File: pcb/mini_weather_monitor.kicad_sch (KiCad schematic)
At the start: 20 parts, among them U2 4.0inch_SPI_MSP4021, U2_BME280 module_bme280, U3_BH1750 module_bh1750

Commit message: working code. pcb wip
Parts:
- removed 5V_buck_boost1: ~, regulator_voltage:S09_HVN, symbol voltage_regulator:S09_HVN
- removed D2, D3, D4, D5, D6: 1N5819, Diode_SMD:D_SOD-123, symbol Diode:1N5819
- added C4: 100nF, Capacitor_SMD:C_1206_3216Metric_Pad1.33x1.80mm_HandSolder, symbol Device:C_Small
- added C5, C6, C7, C8: 10uF, Capacitor_SMD:C_1206_3216Metric_Pad1.33x1.80mm_HandSolder, symbol Device:C_Small
- added J1: Conn_01x02, Connector_PinHeader_2.54mm:PinHeader_1x02_P2.54mm_Vertical, symbol Connector_Generic:Conn_01x02
- added Q1: IRLML6402, Package_TO_SOT_SMD:SOT-23, symbol Transistor_FET:IRLML6402
- added R2: 1k, Resistor_SMD:R_1206_3216Metric, symbol Device:R
- added U1: ~, boost_converter:Pololu U3V70F5, symbol buck_converter:U3V70F5
- C1, C2, C3: value C_Small -> 100nF
- D1: footprint Diode_SMD:D_SOD-123 -> Diode_SMD:D_SMB
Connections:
- net +3V3: now also C4.1, C7.1
- net GND: now also C1.2, C2.2, C3.2, C4.2, C5.2, C6.2, C7.2, C8.2, R2.2, U1.2 (GND), U1.4 (GND)
- net VCC: now also C1.1, C3.1, U2.1 (VCC), U3_BH1750.5 (VCC), C5.1, C6.1, C8.1, U1.5 (VOUT); no longer C2.2
- net VBUS: now reaches D1.1 (K)
- net VBUS: now also Q1.2 (S), U1.3 (VIN)
- net at adafruit_type_c_breakout_rev_b1.2 (VBUS): now also adafruit_type_c_vertical_breakout1.10 (VBUS), adafruit_type_c_vertical_breakout1.2 (VBUS), Q1.3 (D)
- net at D1.2 (A): now also Q1.1 (G), R2.1; no longer adafruit_type_c_vertical_breakout1.2 (VBUS)
- net at U_ESP32_DEVKIT_V1.12 (RX0): now also J1.1 (Pin_1)
- net at U_ESP32_DEVKIT_V1.13 (TX0): now also J1.2 (Pin_2)
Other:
- moved on the sheet: C1, C3, H1, H2

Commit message: set mosfet, schottkey and resistor
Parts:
- D1: footprint Diode_SMD:D_SMB -> Diode_SMD:D_SOD-123
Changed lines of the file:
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@@
 			)
 		)
-		(property "Footprint" "Diode_SMD:D_SMB"
+		(property "Footprint" "Diode_SMD:D_SOD-123"
 			(at 31.75 63.5 0)
 			(effects

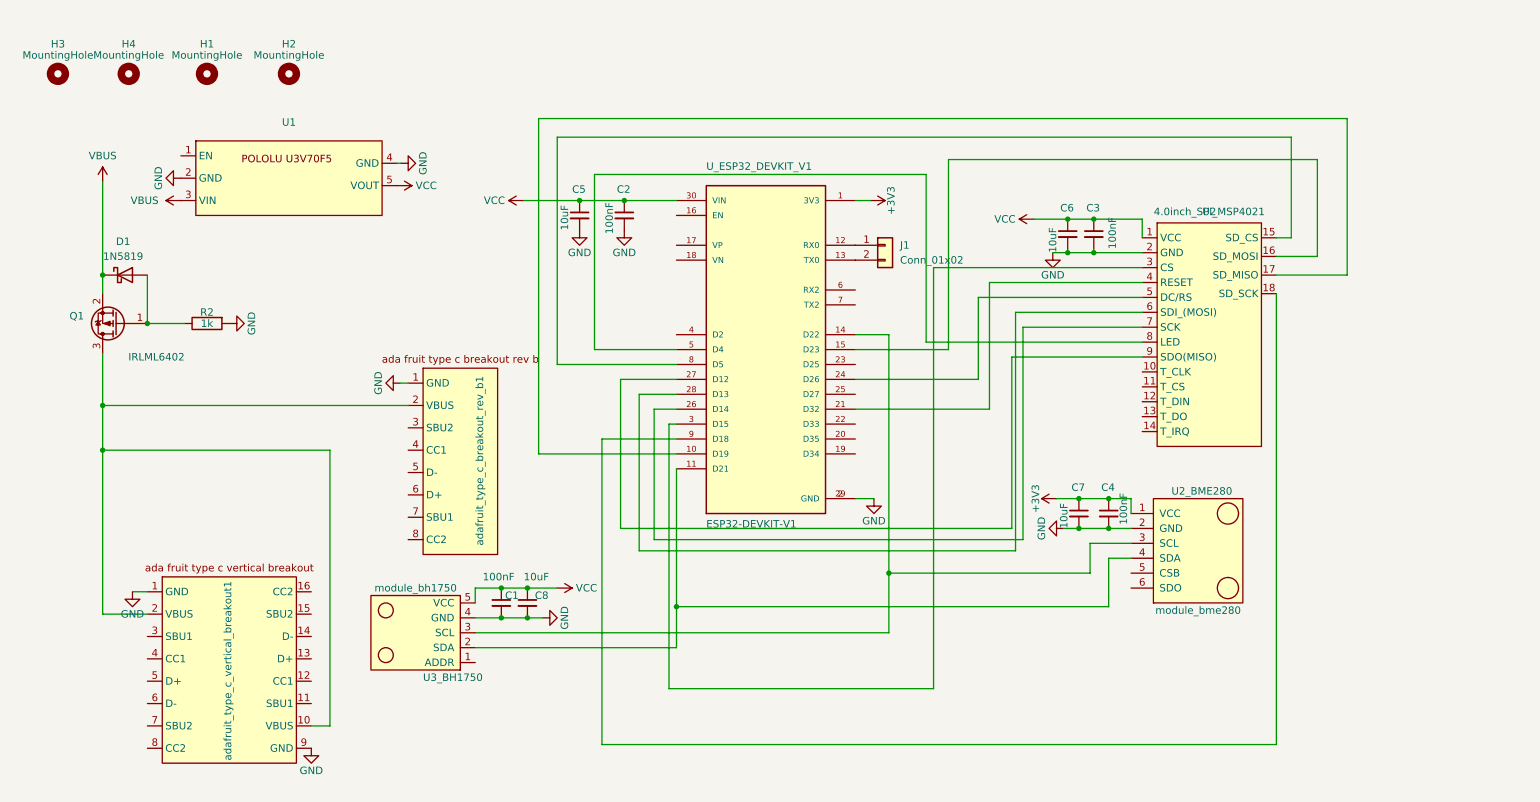
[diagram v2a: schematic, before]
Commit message: adding mini sdcard to use instead of onboard sdcard
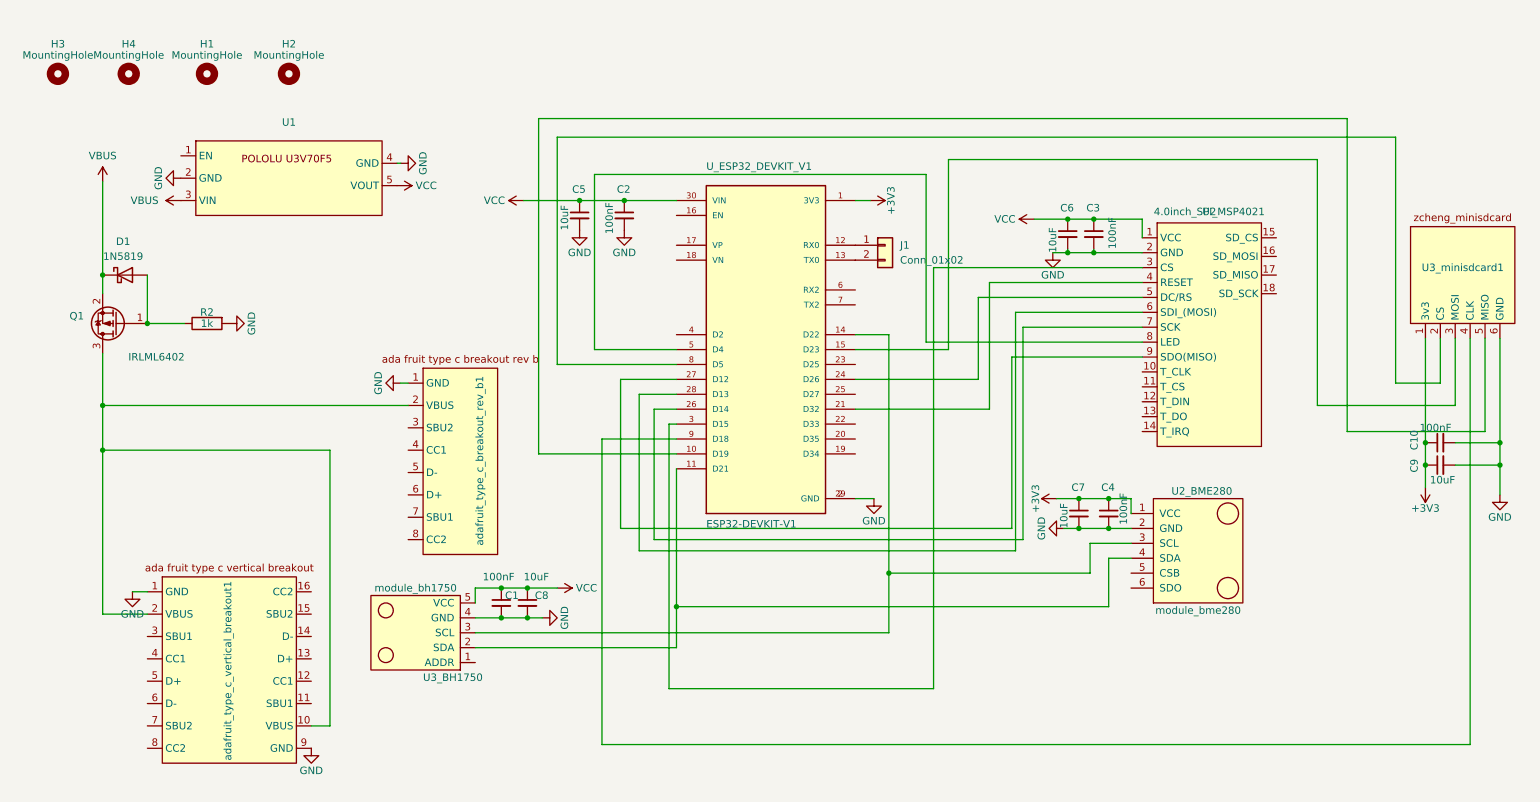
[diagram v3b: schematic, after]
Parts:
- added C10: 100nF, Capacitor_SMD:C_1206_3216Metric_Pad1.33x1.80mm_HandSolder, symbol Device:C_Small
- added C9: 10uF, Capacitor_SMD:C_1206_3216Metric_Pad1.33x1.80mm_HandSolder, symbol Device:C_Small
- added U3_minisdcard1: ~, mini_weather_monitor:zicheng_mini_sd_card_reader, symbol zicheng_minisdcard:zicheng_minisdcard
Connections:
- net +3V3: now also C10.1, C9.1, U3_minisdcard1.1 (3v3)
- net GND: now also C10.2, C9.2, U3_minisdcard1.6 (GND)
- net at U2.15 (SD_CS): no longer U_ESP32_DEVKIT_V1.8 (D5)
- net at U2.16 (SD_MOSI): no longer U_ESP32_DEVKIT_V1.15 (D23)
- net at U2.17 (SD_MISO): no longer U_ESP32_DEVKIT_V1.10 (D19)
- net at U2.18 (SD_SCK): no longer U_ESP32_DEVKIT_V1.9 (D18)
- new net: U3_minisdcard1.5 (MISO), U_ESP32_DEVKIT_V1.10 (D19)
- new net: U3_minisdcard1.3 (MOSI), U_ESP32_DEVKIT_V1.15 (D23)
- new net: U3_minisdcard1.2 (CS), U_ESP32_DEVKIT_V1.8 (D5)
- new net: U3_minisdcard1.4 (CLK), U_ESP32_DEVKIT_V1.9 (D18)

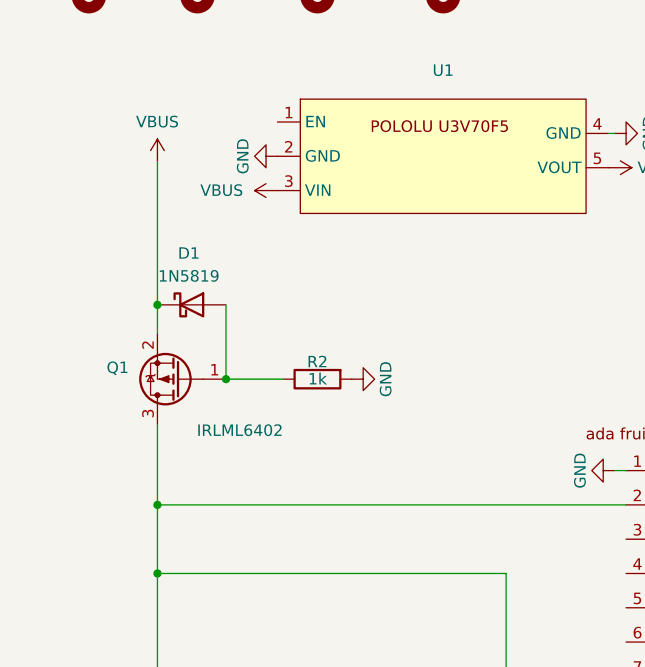
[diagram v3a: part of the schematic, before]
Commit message: moved config info to config on sdcard
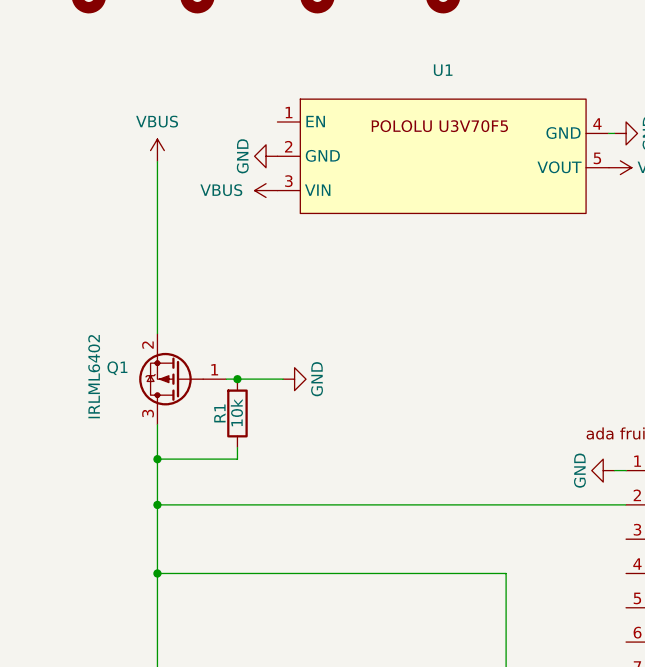
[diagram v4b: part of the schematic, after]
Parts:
- removed D1: 1N5819, Diode_SMD:D_SOD-123, symbol Diode:1N5819
- removed R2: 1k, Resistor_SMD:R_1206_3216Metric, symbol Device:R
- added R1: 10k, Resistor_SMD:R_1206_3216Metric, symbol Device:R
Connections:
- net GND: now also Q1.1 (G), R1.2
- net at Q1.3 (D), adafruit_type_c_breakout_rev_b1.2 (VBUS), adafruit_type_c_vertical_breakout1.10 (VBUS)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: now also R1.1
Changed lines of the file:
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@@
 	)
 	(junction
-		(at 35.56 67.31)
-		(diameter 0)
-		(color 0 0 0 0)
-	)
-	(junction
 		(at 194.31 102.235)
 		(diameter 0)
@@
 	)
 	(junction
-		(at 253.365 91.44)
+		(at 27.94 76.2)
 		(diameter 0)
 		(color 0 0 0 0)
 	)
 	(junction
-		(at 266.065 87.63)
+		(at 253.365 91.44)
 		(diameter 0)
 		(color 0 0 0 0)
 	)
 	(junction
-		(at 27.94 59.055)
+		(at 266.065 87.63)
 		(diameter 0)
 		(color 0 0 0 0)
@@
 	)
 	(junction
+		(at 36.83 67.31)
+		(diameter 0)
+		(color 0 0 0 0)
+	)
+	(junction
 		(at 196.85 55.245)
 		(diameter 0)
@@
 	(wire
 		(pts
-			(xy 27.94 59.055) (xy 27.94 62.23)
+			(xy 27.94 43.18) (xy 27.94 62.23)
 		)
 		(stroke
@@
 	(wire
 		(pts
-			(xy 27.94 72.39) (xy 27.94 81.28)
+			(xy 27.94 72.39) (xy 27.94 76.2)
 		)
 		(stroke
@@
 	(wire
 		(pts
-			(xy 27.94 43.18) (xy 27.94 59.055)
+			(xy 41.91 67.31) (xy 36.83 67.31)
 		)
 		(stroke
@@
 	(wire
 		(pts
-			(xy 41.91 67.31) (xy 35.56 67.31)
+			(xy 248.285 35.56) (xy 248.285 77.47)
 		)
 		(stroke
@@
 	(wire
 		(pts
-			(xy 248.285 35.56) (xy 248.285 77.47)
+			(xy 169.545 129.54) (xy 124.46 129.54)
 		)
 		(stroke
@@
 	(wire
 		(pts
-			(xy 169.545 129.54) (xy 124.46 129.54)
+			(xy 203.2 104.775) (xy 196.215 104.775)
 		)
 		(stroke
@@
 	(wire
 		(pts
-			(xy 203.2 104.775) (xy 196.215 104.775)
+			(xy 36.83 67.31) (xy 35.56 67.31)
 		)
 		(stroke
@@
 	(wire
 		(pts
-			(xy 35.56 59.055) (xy 35.56 67.31)
+			(xy 91.44 112.395) (xy 91.44 114.935)
 		)
 		(stroke
@@
 	(wire
 		(pts
-			(xy 91.44 112.395) (xy 91.44 114.935)
+			(xy 168.275 70.485) (xy 205.105 70.485)
 		)
 		(stroke
@@
 	(wire
 		(pts
-			(xy 168.275 70.485) (xy 205.105 70.485)
+			(xy 189.865 55.245) (xy 192.405 55.245)
 		)
 		(stroke
@@
 	(wire
 		(pts
-			(xy 189.865 55.245) (xy 192.405 55.245)
+			(xy 234.95 81.28) (xy 258.445 81.28)
 		)
 		(stroke
@@
 	(wire
 		(pts
-			(xy 234.95 81.28) (xy 258.445 81.28)
+			(xy 196.85 55.245) (xy 205.105 55.245)
 		)
 		(stroke
@@
 	(wire
 		(pts
-			(xy 196.85 55.245) (xy 205.105 55.245)
+			(xy 116.205 102.235) (xy 116.205 76.835)
 		)
 		(stroke
@@
 	(wire
 		(pts
-			(xy 116.205 102.235) (xy 116.205 76.835)
+			(xy 113.03 86.995) (xy 125.73 86.995)
 		)
 		(stroke
@@
 	(wire
 		(pts
-			(xy 113.03 86.995) (xy 125.73 86.995)
+			(xy 27.94 76.2) (xy 27.94 81.28)
 		)
 		(stroke
@@
 	(wire
 		(pts
+			(xy 36.83 76.2) (xy 27.94 76.2)
+		)
+		(stroke
+			(width 0)
+			(type default)
+		)
+	)
+	(wire
+		(pts
 			(xy 121.92 81.915) (xy 125.73 81.915)
 		)
@@
 	(wire
 		(pts
+			(xy 36.83 74.93) (xy 36.83 76.2)
+		)
+		(stroke
+			(width 0)
+			(type default)
+		)
+	)
+	(wire
+		(pts
 			(xy 156.21 46.355) (xy 158.75 46.355)
 		)
@@
 	(symbol
 		(lib_id "power:GND")
-		(at 49.53 67.31 90)
+		(at 41.91 67.31 90)
 		(unit 1)
 		(exclude_from_sim no)
@@
 		(dnp no)
 		(property "Reference" "#PWR015"
-			(at 55.88 67.31 0)
+			(at 48.26 67.31 0)
 			(effects
 				(font
@@
 		)
 		(property "Value" "GND"
-			(at 53.34 67.31 0)
+			(at 45.72 67.31 0)
 			(effects
 				(font
@@
 		)
 		(property "Footprint" ""
-			(at 49.53 67.31 0)
+			(at 41.91 67.31 0)
 			(effects
 				(font
@@
 		)
 		(property "Datasheet" ""
-			(at 49.53 67.31 0)
+			(at 41.91 67.31 0)
 			(effects
 				(font
@@
 		)
 		(property "Description" ""
-			(at 49.53 67.31 0)
+			(at 41.91 67.31 0)
 			(effects
 				(font
@@
 	)
 	(symbol
+		(lib_id "Device:R")
+		(at 36.83 71.12 0)
+		(mirror x)
+		(unit 1)
+		(exclude_from_sim no)
+		(in_bom yes)
+		(on_board yes)
+		(dnp no)
+		(property "Reference" "R1"
+			(at 34.925 71.12 90)
+			(effects
+				(font
+					(size 1.27 1.27)
+				)
+			)
+		)
+		(property "Value" "10k"
+			(at 36.83 71.12 90)
+			(effects
+				(font
+					(size 1.27 1.27)
+				)
+			)
+		)
+		(property "Footprint" "Resistor_SMD:R_1206_3216Metric"
+			(at 35.052 71.12 90)
+			(effects
+				(font
+					(size 1.27 1.27)
+				)
+				(hide yes)
+			)
+		)
+		(property "Datasheet" "~"
+			(at 36.83 71.12 0)
+			(effects
+				(font
+					(size 1.27 1.27)
+				)
+				(hide yes)
+			)
+		)
+		(property "Description" "Resistor"
+			(at 36.83 71.12 0)
+			(effects
+				(font
+					(size 1.27 1.27)
+				)
+				(hide yes)
+			)
+		)
+		(pin "1"
+		)
+		(pin "2"
+		)
+		(instances
+			(project "mini_weather_monitor"
+				(path "/e63e39d7-6ac0-4ffd-8aa3-1841a4541b55"
+					(reference "R1")
+					(unit 1)
+				)
+			)
+		)
+	)
+	(symbol
 		(lib_id "power:GND")
 		(at 78.74 77.47 270)
@@
 	)
 	(symbol
-		(lib_id "Diode:1N5819")
-		(at 31.75 59.055 0)
-		(unit 1)
-		(exclude_from_sim no)
-		(in_bom yes)
-		(on_board yes)
-		(dnp no)
-		(fields_autoplaced yes)
-		(property "Reference" "D1"
-			(at 31.4325 53.34 0)
-			(effects
-				(font
-					(size 1.27 1.27)
-				)
-			)
-		)
-		(property "Value" "1N5819"
-			(at 31.4325 55.88 0)
-			(effects
-				(font
-					(size 1.27 1.27)
-				)
-			)
-		)
-		(property "Footprint" "Diode_SMD:D_SOD-123"
-			(at 31.75 63.5 0)
-			(effects
-				(font
-					(size 1.27 1.27)
-				)
-				(hide yes)
-			)
-		)
-		(property "Datasheet" "http://www.vishay.com/docs/88525/1n5817.pdf"
-			(at 31.75 59.055 0)
-			(effects
-				(font
-					(size 1.27 1.27)
-				)
-				(hide yes)
-			)
-		)
-		(property "Description" "40V 1A Schottky Barrier Rectifier Diode, DO-41"
-			(at 31.75 59.055 0)
-			(effects
-				(font
-					(size 1.27 1.27)
-				)
-				(hide yes)
-			)
-		)
-		(pin "2"
-		)
-		(pin "1"
-		)
-		(instances
-			(project "mini_weather_monitor"
-				(path "/e63e39d7-6ac0-4ffd-8aa3-1841a4541b55"
-					(reference "D1")
-					(unit 1)
-				)
-			)
-		)
-	)
-	(symbol
 		(lib_id "Device:C_Small")
 		(at 116.84 48.895 0)
@@
 		)
 		(property "Value" "IRLML6402"
-			(at 41.91 73.025 0)
+			(at 20.955 62.23 90)
 			(effects
 				(font
@@
 					(unit 1)
 				)
-			)
-		)
-	)
-	(symbol
-		(lib_id "Device:R")
-		(at 45.72 67.31 90)
-		(mirror x)
-		(unit 1)
-		(exclude_from_sim no)
-		(in_bom yes)
-		(on_board yes)
-		(dnp no)
-		(property "Reference" "R2"
-			(at 45.72 65.405 90)
-			(effects
-				(font
-					(size 1.27 1.27)
-				)
-			)
-		)
-		(property "Value" "1k"
-			(at 45.72 67.31 90)
-			(effects
-				(font
-					(size 1.27 1.27)
-				)
-			)
-		)
-		(property "Footprint" "Resistor_SMD:R_1206_3216Metric"
-			(at 45.72 65.532 90)
-			(effects
-				(font
-					(size 1.27 1.27)
-				)
-				(hide yes)
-			)
-		)
-		(property "Datasheet" "~"
-			(at 45.72 67.31 0)
-			(effects
-				(font
-					(size 1.27 1.27)
-				)
-				(hide yes)
-			)
-		)
-		(property "Description" "Resistor"
-			(at 45.72 67.31 0)
-			(effects
-				(font
-					(size 1.27 1.27)
-				)
-				(hide yes)
-			)
-		)
-		(pin "1"
-		)
-		(pin "2"
-		)
-		(instances
-			(project "mini_weather_monitor"
-				(path "/e63e39d7-6ac0-4ffd-8aa3-1841a4541b55"
-					(reference "R2")
-					(unit 1)
-				)
